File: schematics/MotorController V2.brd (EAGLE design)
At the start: 120.6 x 100 mm, 53 parts, among them IC1 7805, Q1 BC307

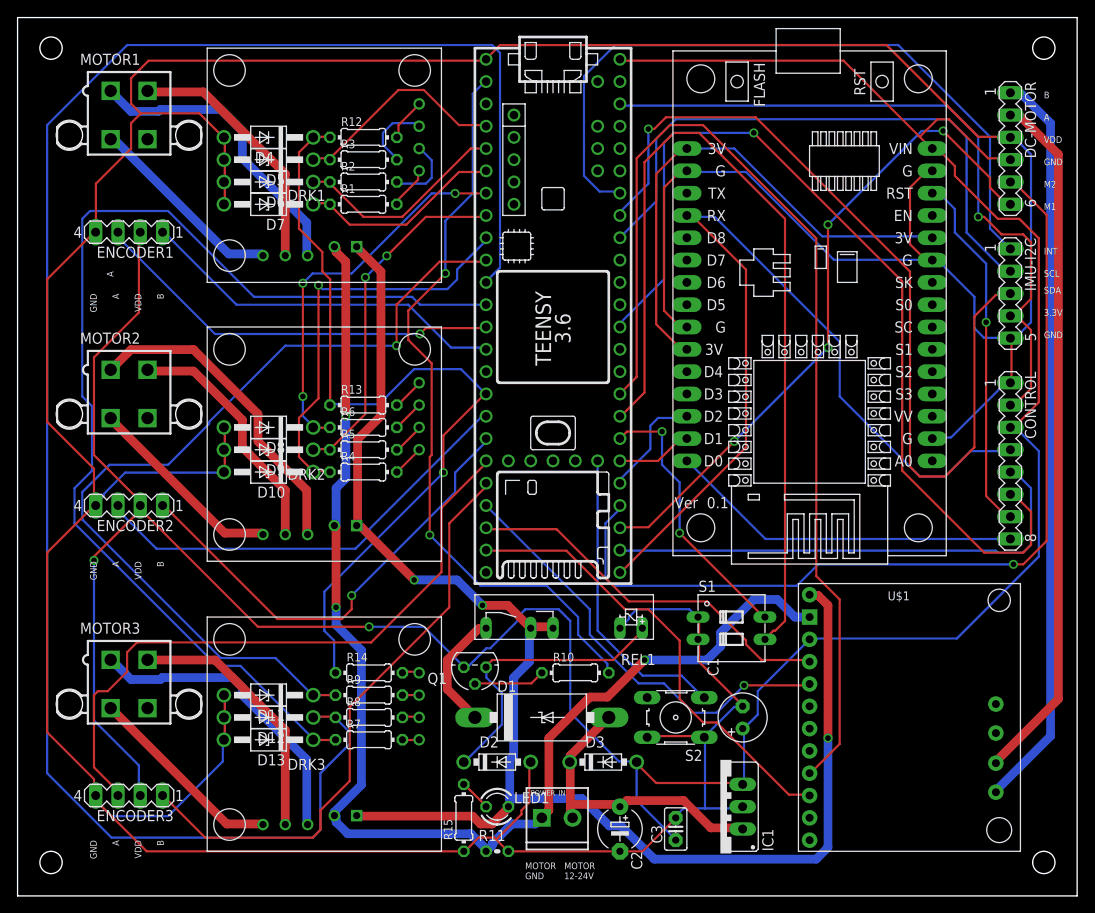
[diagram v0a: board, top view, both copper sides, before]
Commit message: new class I2CMaster
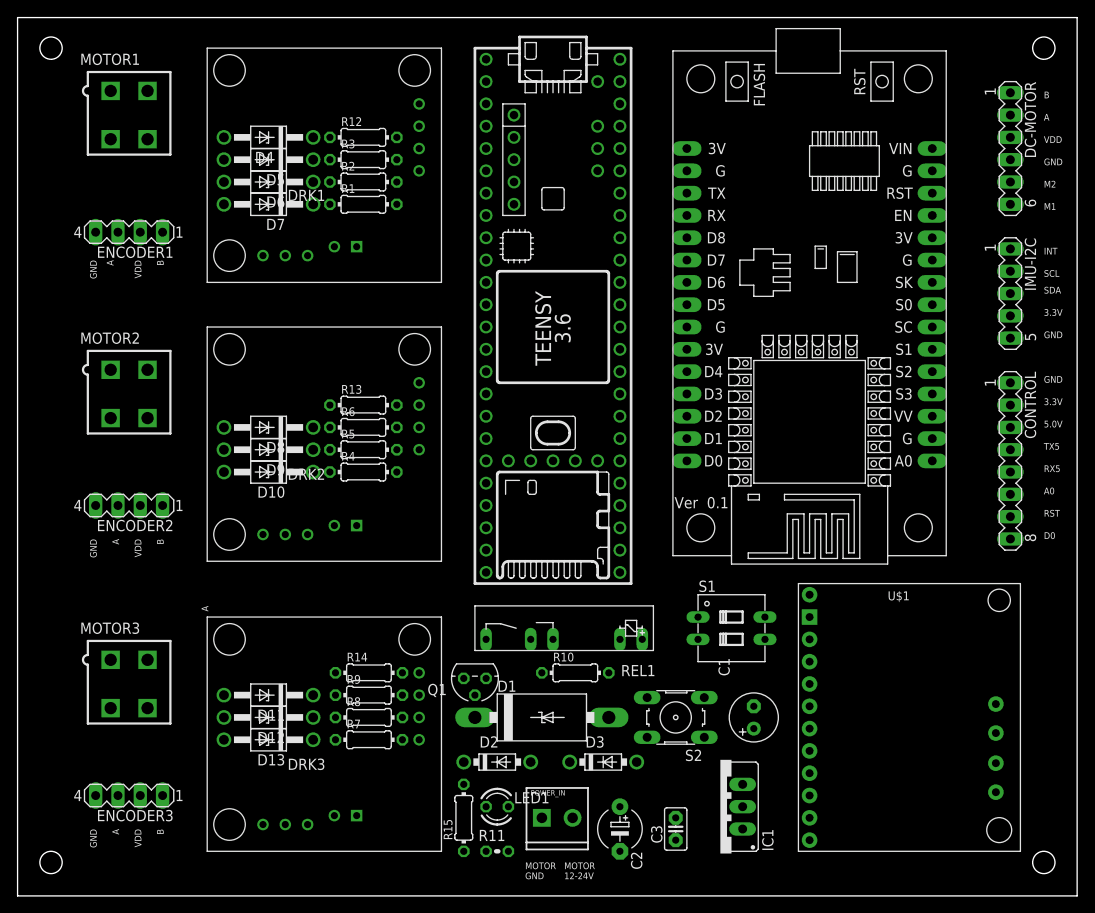
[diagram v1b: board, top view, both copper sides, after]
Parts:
- moved REL1 1.27 mm to (-11.4, 15.2)
- moved C1 1.27 mm to (8.89, 6.35)
- moved Q1 1.27 mm to (-22.9, 10.8)
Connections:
- net N$33 renamed ENC1_A
- net N$34 renamed ENC1_B
- net N$35 renamed ENC2_A
- net N$36 renamed ENC2_B
- net N$37 renamed ENC3_A
- net N$38 renamed ENC3_B
- net N$49 renamed D0
- net N$50 renamed RST
- net N$51 renamed A0
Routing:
- net GND: track 522.6 -> 0.00 mm
- net +5V: track 337.3 -> 0.00 mm, vias 2 -> 0
- net N$28: track 208.2 -> 0.00 mm
- net LIPO-VDD: track 171.2 -> 0.00 mm, vias 3 -> 0
- net LIPO-GND: track 143.4 -> 0.00 mm, vias 3 -> 0
- net N$29: track 126.7 -> 0.00 mm
- net N$60: track 118.4 -> 0.00 mm
- net A0: track 105.1 -> 0.00 mm, vias 1 -> 0
- net Y_ENC_A: track 104.5 -> 0.00 mm, vias 1 -> 0
- net TX5: track 103.9 -> 0.00 mm
- net N$12: track 100.5 -> 0.00 mm
- net IMU-SDA: track 100.3 -> 0.00 mm, vias 1 -> 0
- net N$27: track 100.0 -> 0.00 mm, vias 1 -> 0
- net N$46: track 95.2 -> 0.00 mm, vias 1 -> 0
- net N$42: track 85.1 -> 0.00 mm, vias 2 -> 0
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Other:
- board text added: "5.0V"
- board text added: "A0"
- board text added: "D0"
- board text added: "RST"
- board text added: "RX5"
- board text added: "TX5"

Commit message: ordered PCB !
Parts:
- moved C2 1.42 mm to (-5.08, -5.71)
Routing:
- net GND: track 0.00 -> 489.7 mm, vias 0 -> 1
- net +5V: track 0.00 -> 424.4 mm, vias 0 -> 1
- net N$60: track 0.00 -> 184.2 mm, vias 0 -> 1
- net LIPO-GND: track 0.00 -> 161.5 mm, vias 0 -> 1
- net N$27: track 0.00 -> 146.2 mm
- net LIPO-VDD: track 0.00 -> 133.1 mm, vias 0 -> 3
- net TX5: track 0.00 -> 108.0 mm
- net N$12: track 0.00 -> 102.8 mm
- net N$42: track 0.00 -> 99.6 mm, vias 0 -> 3
- net N$40: track 0.00 -> 98.5 mm
- net BLCK-M2: track 0.00 -> 92.9 mm, vias 0 -> 1
- net Y_ENC_A: track 0.00 -> 92.6 mm, vias 0 -> 1
- net N$46: track 0.00 -> 90.1 mm, vias 0 -> 1
- net WH_ENC_B: track 0.00 -> 88.5 mm, vias 0 -> 2
- net A0: track 0.00 -> 88.2 mm, vias 0 -> 2
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
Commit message: no message
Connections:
- net IMU-SCL: now also IMU-I2C.3, PRJ1.19/A5/SCL; no longer IMU-I2C.2, PRJ1.18/A4/SDA
- net IMU-SDA: now also IMU-I2C.2, PRJ1.18/A4/SDA; no longer IMU-I2C.3, PRJ1.19/A5/SCL
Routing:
- net IMU-SDA: track 71.1 -> 69.4 mm, vias 2 -> 0
- net IMU-SCL: track 69.4 -> 71.1 mm, vias 0 -> 2
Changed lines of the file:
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@@
 <text x="41.91" y="49.53" size="0.762" layer="25">GND</text>
 <text x="41.91" y="52.07" size="0.762" layer="25">3.3V</text>
-<text x="41.91" y="54.61" size="0.762" layer="25">SDA</text>
-<text x="41.91" y="56.8325" size="0.762" layer="25">SCL</text>
+<text x="41.91" y="56.515" size="0.762" layer="25">SDA</text>
+<text x="41.91" y="54.9275" size="0.762" layer="25">SCL</text>
 <text x="41.91" y="59.3725" size="0.762" layer="25">INT</text>
 <text x="41.91" y="72.0725" size="0.762" layer="25">VDD</text>
@@
 <via x="-39.5605" y="-2.667" extent="1-16" drill="0.635"/>
 </signal>
-<signal name="IMU-SDA">
+<signal name="IMU-SCL">
 <contactref element="IMU-I2C" pad="3"/>
 <contactref element="PRJ1" pad="19/A5/SCL"/>
@@
 <wire x1="-6.223" y1="22.89175" x2="-6.35" y2="22.86" width="0.254" layer="16"/>
 </signal>
-<signal name="IMU-SCL">
+<signal name="IMU-SDA">
 <contactref element="PRJ1" pad="18/A4/SDA"/>
 <contactref element="IMU-I2C" pad="2"/>
@@
 </signal>
 <signal name="3V">
-<contactref element="U$3" pad="11"/>
-<contactref element="U$3" pad="16"/>
-<contactref element="U$3" pad="25"/>
 <wire x1="2.2225" y1="48.4505" x2="1.3335" y2="48.4505" width="0.254" layer="16"/>
 <wire x1="3.77825" y1="50.00625" x2="2.2225" y2="48.4505" width="0.254" layer="16"/>
@@
 <wire x1="3.77825" y1="61.11875" x2="29.11475" y2="61.11875" width="0.254" layer="16"/>
 <wire x1="29.11475" y1="61.11875" x2="29.21" y2="60.96" width="0.254" layer="16"/>
+<contactref element="U$3" pad="11"/>
+<contactref element="U$3" pad="16"/>
+<contactref element="U$3" pad="25"/>
 </signal>
 <signal name="N$41">
